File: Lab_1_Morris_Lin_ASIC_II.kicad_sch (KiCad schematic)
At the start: 96 parts, among them IC1 74CBTLV3253D,118, IC2 74CBTLV3253D,118, IC3 74CBTLV3253D,118, IC4 74CBTLV3253D,118, IC5 74CBTLV3253D,118, IC6 74CBTLV3253D,118, J1 VDDPST_External, J2 PMOD_A, J3 PMOD_B, J4 VDD_Qn External, J5 VDDPST External, J6 PMOD_A, J7 PMOD_B, Q1 BSS138, U1 TLV75710PDBV, U2 TLV75710PDBV

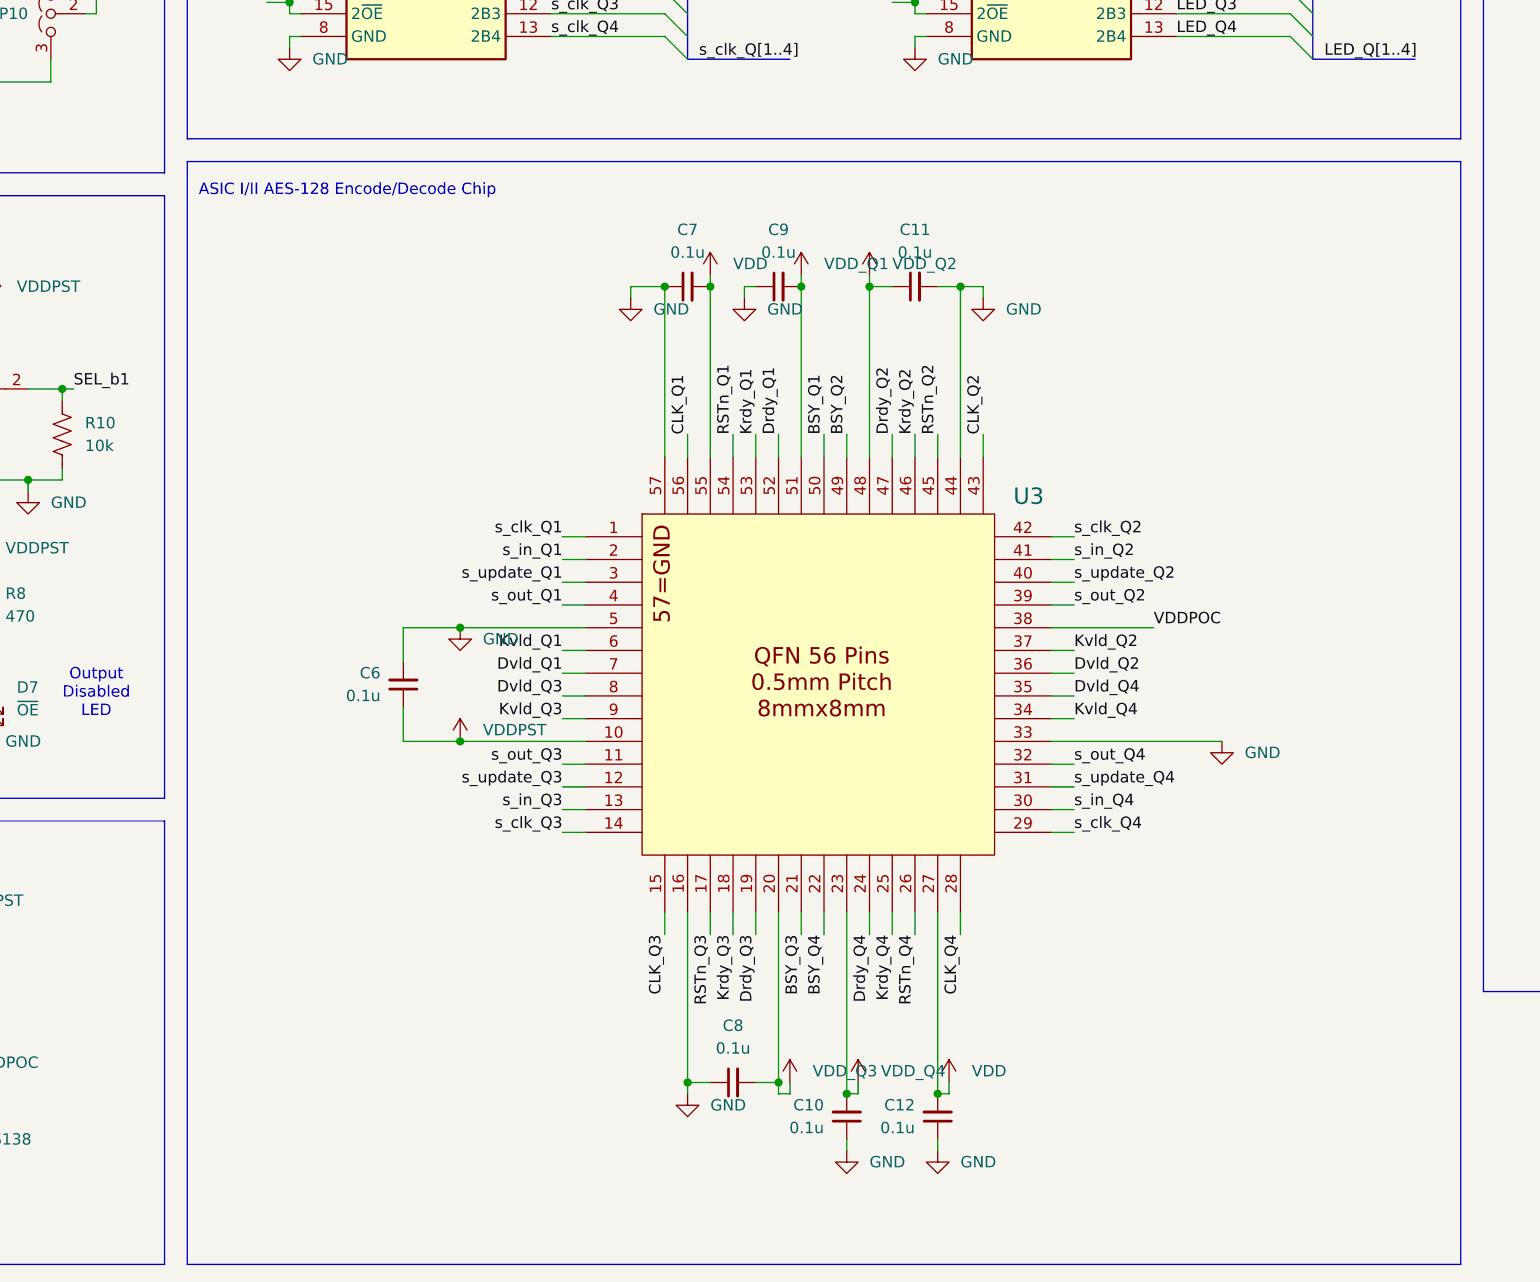
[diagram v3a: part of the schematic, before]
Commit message: Fanned out ASIC pins
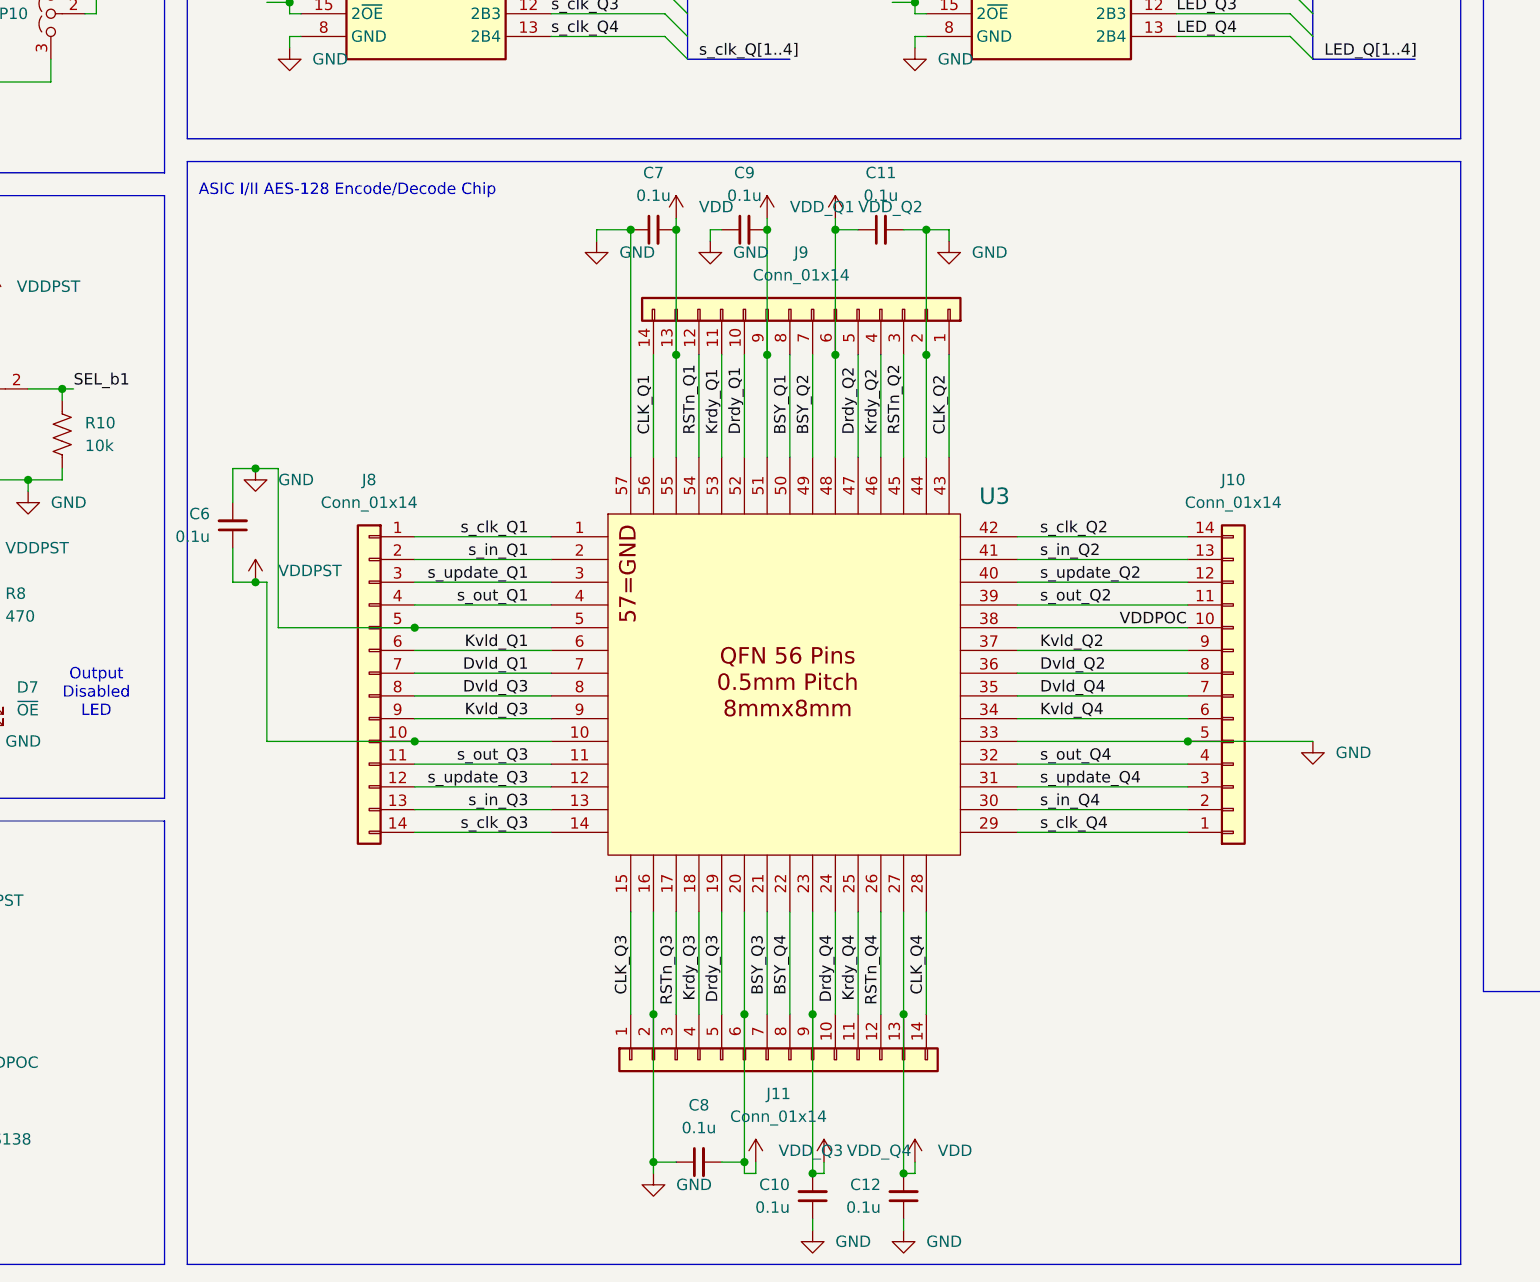
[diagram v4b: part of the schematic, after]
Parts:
- added J10, J11, J8, J9: Conn_01x14, Connector_PinHeader_2.54mm:PinHeader_1x14_P2.54mm_Vertical, symbol Connector_Generic:Conn_01x14
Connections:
- net BSY_Q1: now also J9.8 (Pin_8)
- net BSY_Q2: now also J9.7 (Pin_7)
- net BSY_Q3: now also J11.7 (Pin_7)
- net BSY_Q4: now also J11.8 (Pin_8)
- net CLK_Q1: now also J9.14 (Pin_14)
- net CLK_Q2: now also J9.1 (Pin_1)
- net CLK_Q3: now also J11.1 (Pin_1)
- net CLK_Q4: now also J11.14 (Pin_14)
- net Drdy_Q1: now also J9.10 (Pin_10)
- net Drdy_Q2: now also J9.5 (Pin_5)
- net Drdy_Q3: now also J11.5 (Pin_5)
- net Drdy_Q4: now also J11.10 (Pin_10)
- net Dvld_Q1: now also J8.7 (Pin_7)
- net Dvld_Q2: now also J10.8 (Pin_8)
- net Dvld_Q3: now also J8.8 (Pin_8)
- net Dvld_Q4: now also J10.7 (Pin_7)
- net GND: now also J10.5 (Pin_5), J11.2 (Pin_2), J8.5 (Pin_5), J9.2 (Pin_2)
- net Krdy_Q1: now also J9.11 (Pin_11)
- net Krdy_Q2: now also J9.4 (Pin_4)
- net Krdy_Q3: now also J11.4 (Pin_4)
- net Krdy_Q4: now also J11.11 (Pin_11)
- net Kvld_Q1: now also J8.6 (Pin_6)
- net Kvld_Q2: now also J10.9 (Pin_9)
- net Kvld_Q3: now also J8.9 (Pin_9)
- net Kvld_Q4: now also J10.6 (Pin_6)
- net RSTn_Q1: now also J9.12 (Pin_12)
- net RSTn_Q2: now also J9.3 (Pin_3)
- net RSTn_Q3: now also J11.3 (Pin_3)
- net RSTn_Q4: now also J11.12 (Pin_12)
- net VDD: now also J11.13 (Pin_13), J9.13 (Pin_13)
- net VDDPOC: now also J10.10 (Pin_10)
- net VDDPST: now also J8.10 (Pin_10)
- net VDD_Q1: now also J9.9 (Pin_9)
- net VDD_Q2: now also J9.6 (Pin_6)
- net VDD_Q3: now also J11.6 (Pin_6)
- net VDD_Q4: now also J11.9 (Pin_9)
- net s_clk_Q1: now also J8.1 (Pin_1)
- net s_clk_Q2: now also J10.14 (Pin_14)
- net s_clk_Q3: now also J8.14 (Pin_14)
- net s_clk_Q4: now also J10.1 (Pin_1)
- net s_in_Q1: now also J8.2 (Pin_2)
- net s_in_Q2: now also J10.13 (Pin_13)
- net s_in_Q3: now also J8.13 (Pin_13)
- net s_in_Q4: now also J10.2 (Pin_2)
- net s_out_Q1: now also J8.4 (Pin_4)
- net s_out_Q2: now also J10.11 (Pin_11)
- net s_out_Q3: now also J8.11 (Pin_11)
- net s_out_Q4: now also J10.4 (Pin_4)
- net s_update_Q1: now also J8.3 (Pin_3)
- net s_update_Q2: now also J10.12 (Pin_12)
- net s_update_Q3: now also J8.12 (Pin_12)
- net s_update_Q4: now also J10.3 (Pin_3)
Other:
- moved on the sheet: C10, C11, C12, C6, C7, C8, C9, U3

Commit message: auto1 design
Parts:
- removed J1: VDDPST_External, Connector:Banana_Jack_2Pin, symbol Connector_Generic:Conn_01x02
- added J12: VDDPST External, Connector:Banana_Jack_1Pin, symbol Connector_Generic:Conn_01x01
- added J13: GND External, Connector:Banana_Jack_1Pin, symbol Connector_Generic:Conn_01x01
- J5: value VDDPST External -> VDDRING External
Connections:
- net GND: now also J13.1 (Pin_1)
- net VDDPMOD: no longer J2.12 (Pin_12), J3.12 (Pin_12)
- net at JP1.3 (B): now also J12.1 (Pin_1)
- no-connect marks 4 -> 6
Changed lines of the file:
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@@
 	)
 	(junction
-		(at 40.64 205.74)
-		(diameter 0)
-		(color 0 0 0 0)
-	)
-	(junction
 		(at 215.9 120.65)
 		(diameter 0)
@@
 	)
 	(junction
-		(at 40.64 175.26)
-		(diameter 0)
-		(color 0 0 0 0)
-	)
-	(junction
 		(at 142.24 185.42)
 		(diameter 0)
@@
 	)
 	(no_connect
+		(at 53.34 196.85)
+	)
+	(no_connect
+		(at 53.34 166.37)
+	)
+	(no_connect
 		(at 307.34 40.64)
 	)
@@
 	(wire
 		(pts
-			(xy 53.34 196.85) (xy 53.34 205.74)
-		)
-		(stroke
-			(width 0)
-			(type default)
-		)
-	)
-	(wire
-		(pts
 			(xy 86.36 121.92) (xy 85.09 121.92)
 		)
@@
 	(wire
 		(pts
-			(xy 40.64 175.26) (xy 53.34 175.26)
-		)
-		(stroke
-			(width 0)
-			(type default)
-		)
-	)
-	(wire
-		(pts
 			(xy 53.34 161.29) (xy 58.42 161.29)
 		)
@@
 	(wire
 		(pts
-			(xy 30.48 35.56) (xy 30.48 44.45)
+			(xy 30.48 41.91) (xy 30.48 44.45)
 		)
 		(stroke
@@
 	(wire
 		(pts
-			(xy 53.34 166.37) (xy 53.34 175.26)
-		)
-		(stroke
-			(width 0)
-			(type default)
-		)
-	)
-	(wire
-		(pts
 			(xy 22.86 86.36) (xy 34.29 86.36)
 		)
@@
 	(wire
 		(pts
-			(xy 40.64 205.74) (xy 53.34 205.74)
-		)
-		(stroke
-			(width 0)
-			(type default)
-		)
-	)
-	(wire
-		(pts
 			(xy 209.55 146.05) (xy 207.01 146.05)
 		)
@@
 	(wire
 		(pts
-			(xy 30.48 35.56) (xy 29.21 35.56)
+			(xy 30.48 41.91) (xy 29.21 41.91)
 		)
 		(stroke
@@
 	)
 	(symbol
-		(lib_id "Connector_Generic:Conn_01x02")
-		(at 24.13 33.02 0)
-		(mirror y)
-		(unit 1)
-		(body_style 1)
-		(exclude_from_sim no)
-		(in_bom no)
-		(on_board yes)
-		(in_pos_files yes)
-		(dnp no)
-		(fields_autoplaced yes)
-		(property "Reference" "J1"
-			(at 24.13 26.67 0)
-			(show_name no)
-			(do_not_autoplace no)
-			(effects
-				(font
-					(size 1.27 1.27)
-				)
-			)
-		)
-		(property "Value" "VDDPST_External"
-			(at 24.13 29.21 0)
-			(show_name no)
-			(do_not_autoplace no)
-			(effects
-				(font
-					(size 1.27 1.27)
-				)
-			)
-		)
-		(property "Footprint" "Connector:Banana_Jack_2Pin"
-			(at 24.13 33.02 0)
-			(hide yes)
-			(show_name no)
-			(do_not_autoplace no)
-			(effects
-				(font
-					(size 1.27 1.27)
-				)
-			)
-		)
-		(property "Datasheet" ""
-			(at 24.13 33.02 0)
-			(hide yes)
-			(show_name no)
-			(do_not_autoplace no)
-			(effects
-				(font
-					(size 1.27 1.27)
-				)
-			)
-		)
-		(property "Description" "Generic connector, single row, 01x02, script generated (kicad-library-utils/schlib/autogen/connector/)"
-			(at 24.13 33.02 0)
-			(hide yes)
-			(show_name no)
-			(do_not_autoplace no)
-			(effects
-				(font
-					(size 1.27 1.27)
-				)
-			)
-		)
-		(property "KLC_S3.3" ""
-			(at 24.13 33.02 0)
-			(hide yes)
-			(show_name no)
-			(do_not_autoplace no)
-			(effects
-				(font
-					(size 1.27 1.27)
-				)
-			)
-		)
-		(property "KLC_S5.1" ""
-			(at 24.13 33.02 0)
-			(hide yes)
-			(show_name no)
-			(do_not_autoplace no)
-			(effects
-				(font
-					(size 1.27 1.27)
-				)
-			)
-		)
-		(pin "2"
-		)
-		(pin "1"
-		)
-		(instances
-			(project "Lab_1_Morris_Lin_ASIC_II"
-				(path "/fd1324de-06cc-4eb6-9701-e191d26a4c5f"
-					(reference "J1")
-					(unit 1)
-				)
-			)
-		)
-	)
-	(symbol
 		(lib_id "ASIC_II:PTVS3V3S1UR,115")
 		(at 76.2 27.94 270)
@@
 	)
 	(symbol
+		(lib_id "Connector_Generic:Conn_01x01")
+		(at 24.13 41.91 180)
+		(unit 1)
+		(body_style 1)
+		(exclude_from_sim no)
+		(in_bom no)
+		(on_board yes)
+		(in_pos_files yes)
+		(dnp no)
+		(property "Reference" "J13"
+			(at 24.13 35.56 0)
+			(show_name no)
+			(do_not_autoplace no)
+			(effects
+				(font
+					(size 1.27 1.27)
+				)
+			)
+		)
+		(property "Value" "GND External"
+			(at 24.13 38.1 0)
+			(show_name no)
+			(do_not_autoplace no)
+			(effects
+				(font
+					(size 1.27 1.27)
+				)
+			)
+		)
+		(property "Footprint" "Connector:Banana_Jack_1Pin"
+			(at 24.13 41.91 0)
+			(hide yes)
+			(show_name no)
+			(do_not_autoplace no)
+			(effects
+				(font
+					(size 1.27 1.27)
+				)
+			)
+		)
+		(property "Datasheet" ""
+			(at 24.13 41.91 0)
+			(hide yes)
+			(show_name no)
+			(do_not_autoplace no)
+			(effects
+				(font
+					(size 1.27 1.27)
+				)
+			)
+		)
+		(property "Description" "Generic connector, single row, 01x01, script generated (kicad-library-utils/schlib/autogen/connector/)"
+			(at 24.13 41.91 0)
+			(hide yes)
+			(show_name no)
+			(do_not_autoplace no)
+			(effects
+				(font
+					(size 1.27 1.27)
+				)
+			)
+		)
+		(property "KLC_S3.3" ""
+			(at 24.13 41.91 0)
+			(hide yes)
+			(show_name no)
+			(do_not_autoplace no)
+			(effects
+				(font
+					(size 1.27 1.27)
+				)
+			)
+		)
+		(property "KLC_S5.1" ""
+			(at 24.13 41.91 0)
+			(hide yes)
+			(show_name no)
+			(do_not_autoplace no)
+			(effects
+				(font
+					(size 1.27 1.27)
+				)
+			)
+		)
+		(pin "1"
+		)
+		(instances
+			(project "Lab_1_Morris_Lin_ASIC_II"
+				(path "/fd1324de-06cc-4eb6-9701-e191d26a4c5f"
+					(reference "J13")
+					(unit 1)
+				)
+			)
+		)
+	)
+	(symbol
 		(lib_id "power:VDD")
 		(at 24.13 167.64 0)
@@
 			)
 		)
-		(property "Value" "VDDPST External"
+		(property "Value" "VDDRING External"
 			(at 80.01 71.12 0)
 			(show_name no)
@@
 					(unit 1)
 				)
+			)
+		)
+	)
+	(symbol
+		(lib_id "Connector_Generic:Conn_01x01")
+		(at 24.13 33.02 180)
+		(unit 1)
+		(body_style 1)
+		(exclude_from_sim no)
+		(in_bom no)
+		(on_board yes)
+		(in_pos_files yes)
+		(dnp no)
+		(property "Reference" "J12"
+			(at 24.13 26.67 0)
+			(show_name no)
+			(do_not_autoplace no)
+			(effects
+				(font
+					(size 1.27 1.27)
+				)
+			)
+		)
+		(property "Value" "VDDPST External"
+			(at 24.13 29.21 0)
+			(show_name no)
+			(do_not_autoplace no)
+			(effects
+				(font
+					(size 1.27 1.27)
+				)
+			)
+		)
+		(property "Footprint" "Connector:Banana_Jack_1Pin"
+			(at 24.13 33.02 0)
+			(hide yes)
+			(show_name no)
+			(do_not_autoplace no)
+			(effects
+				(font
+					(size 1.27 1.27)
+				)
+			)
+		)
+		(property "Datasheet" ""
+			(at 24.13 33.02 0)
+			(hide yes)
+			(show_name no)
+			(do_not_autoplace no)
+			(effects
+				(font
+					(size 1.27 1.27)
+				)
+			)
+		)
+		(property "Description" "Generic connector, single row, 01x01, script generated (kicad-library-utils/schlib/autogen/connector/)"
+			(at 24.13 33.02 0)
+			(hide yes)
+			(show_name no)
+			(do_not_autoplace no)
+			(effects
+				(font
+					(size 1.27 1.27)
+				)
+			)
+		)
+		(property "KLC_S3.3" ""
+			(at 24.13 33.02 0)
+			(hide yes)
+			(show_name no)
+			(do_not_autoplace no)
+			(effects
+				(font
+					(size 1.27 1.27)
+				)
+			)
+		)
+		(property "KLC_S5.1" ""
+			(at 24.13 33.02 0)
+			(hide yes)
+			(show_name no)
+			(do_not_autoplace no)
+			(effects
+				(font
+					(size 1.27 1.27)
+				)
+			)
+		)
+		(pin "1"
+		)
+		(instances
+			(project "Lab_1_Morris_Lin_ASIC_II"
+				(path "/fd1324de-06cc-4eb6-9701-e191d26a4c5f"
+					(reference "J12")
+					(unit 1)
+				)
